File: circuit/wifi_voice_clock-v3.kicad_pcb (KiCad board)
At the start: 2 copper layers, 38.1 x 220.3 mm, 77 parts, among them J1 PinSocket 1x06 5.7mm, J11 PinHeader 1x10 7.7mm, J12 PinHeader 1x10 7.7mm, J13 PinSocket 1x10 3.5mm, J14 PinSocket 1x10 3.5mm, J15 PinSocket 1x10 3.5mm, J16 PinSocket 1x10 3.5mm, J2 PinSocket 1x08 5.7mm, J21 PinSocket 1x10 3.5mm, J22 PinSocket 1x10 3.5mm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

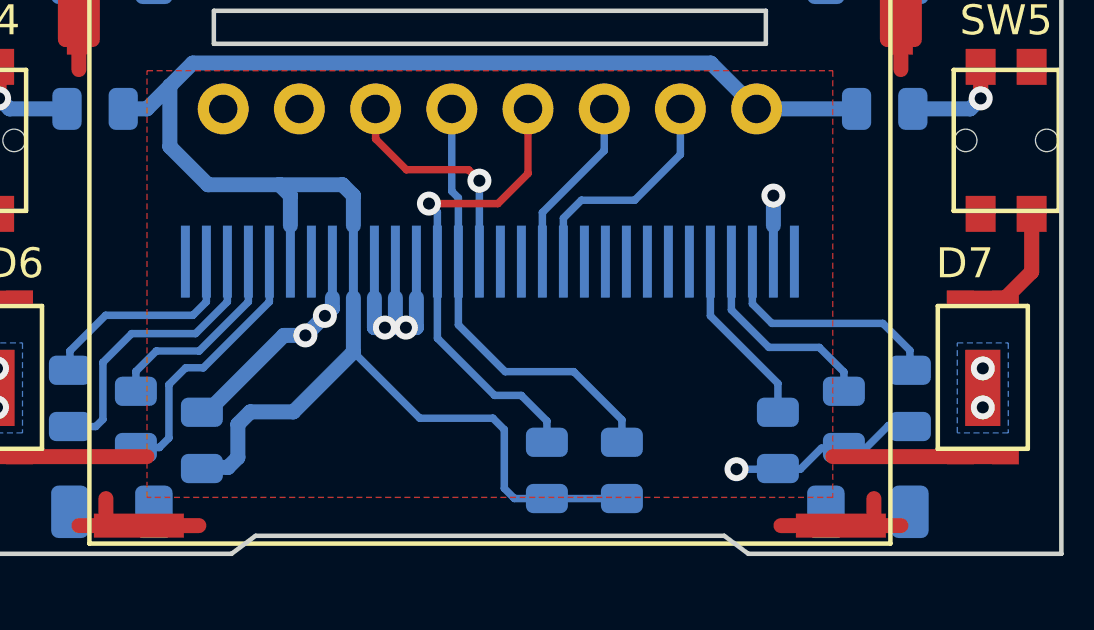
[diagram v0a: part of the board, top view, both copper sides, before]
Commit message: Adjust OLED footprint
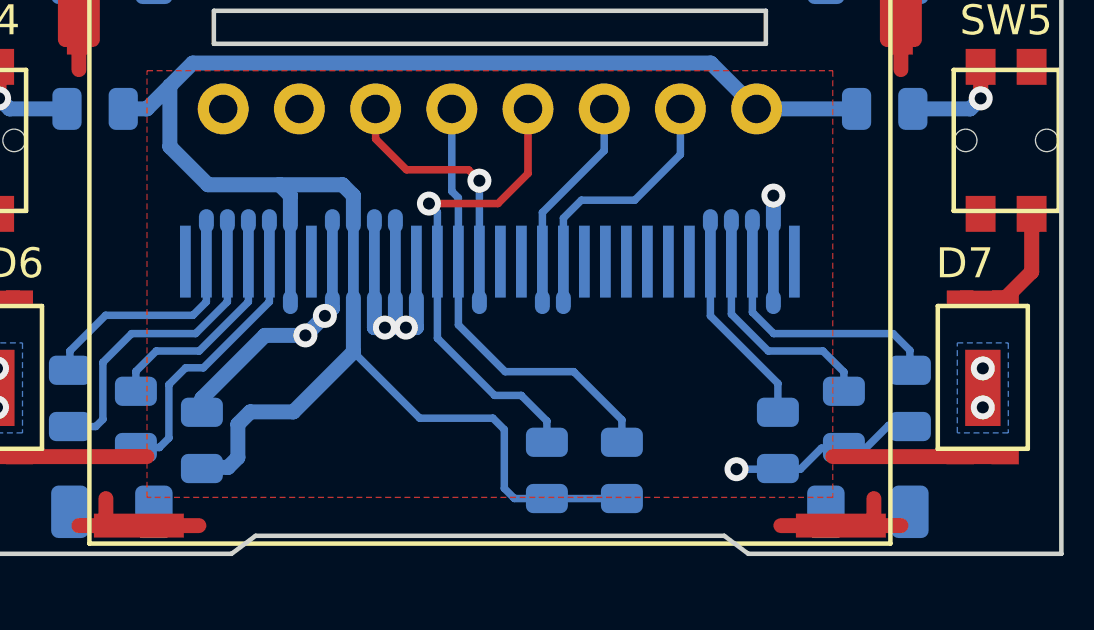
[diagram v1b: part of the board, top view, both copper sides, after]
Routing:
- net /LCD_GND: track 29.5 -> 31.0 mm

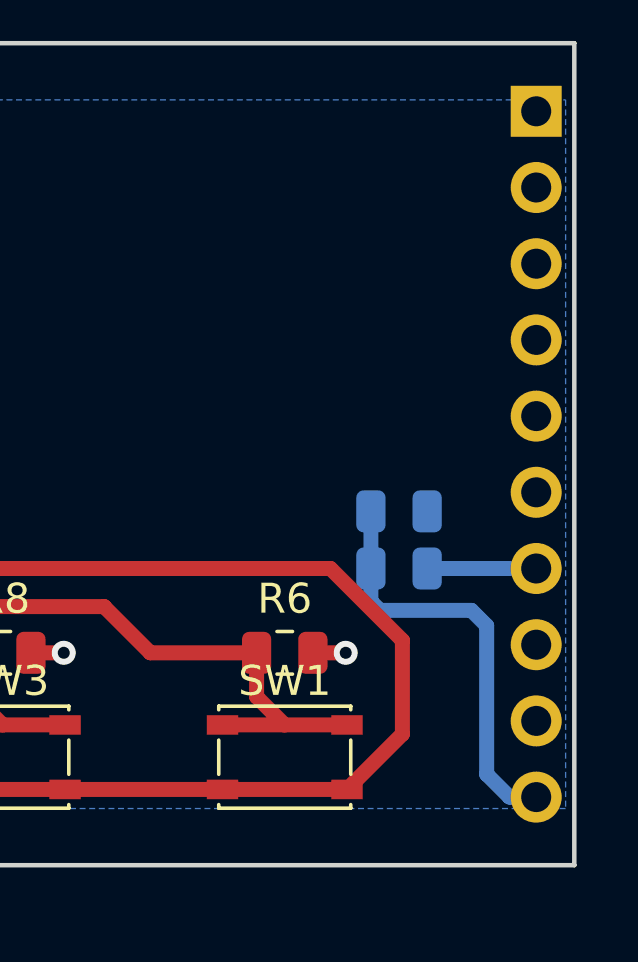
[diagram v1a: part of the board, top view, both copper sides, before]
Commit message: Measure real input voltage
Circuit is from https://jeelabs.org/2013/05/17/zero-powe-battery-measurement/
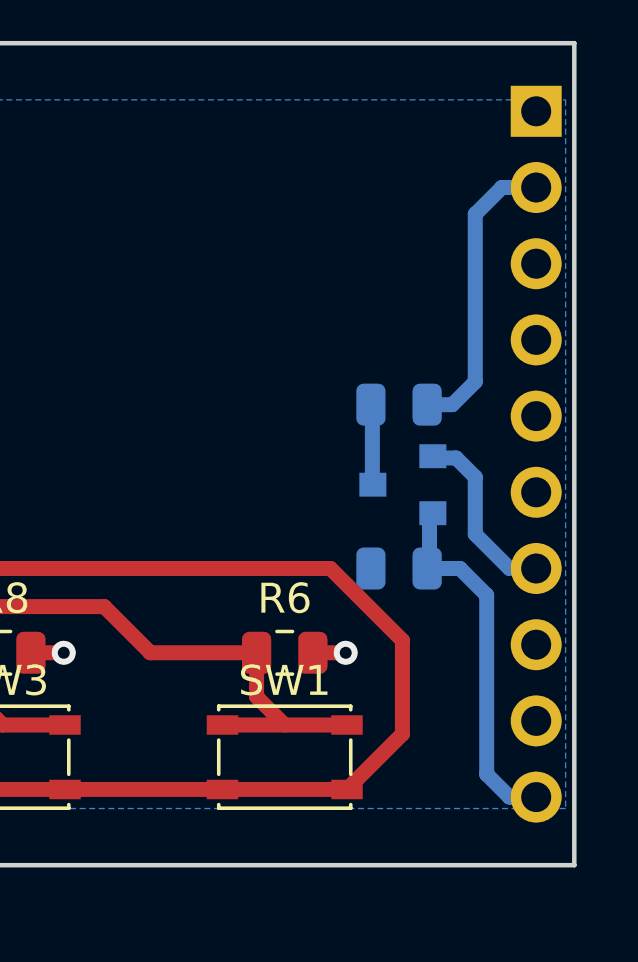
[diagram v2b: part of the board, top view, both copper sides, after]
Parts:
- added Q3: BSS138, Package_TO_SOT_SMD:SOT-23, B.Cu at (13.3, 79.8)
- R9: value 10K -> 40K
- moved R9 5.46 mm to (13.2, 77.1)
- moved R10 1.91 mm to (13.2, 82.5), turned to 0 degrees
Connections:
- R9 pad 1: /CTRL_VMES -> Net-(Q3-Pad3)
- R9 pad 2: /CTRL_VOUT -> /CTRL_VCC
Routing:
- net /CTRL_VCC: track 0.00 -> 9.91 mm
- net Net-(Q3-Pad3): track 0.00 -> 2.67 mm
- net /CTRL_VOUT: track 3.63 -> 6.20 mm
- net /CTRL_VMES: track 14.3 -> 12.1 mm
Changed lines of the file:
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@@
     (thickness 1)
     (drawings 68)
-    (tracks 503)
+    (tracks 511)
     (zones 0)
-    (modules 77)
-    (nets 139)
+    (modules 78)
+    (nets 140)
   )
   (page A4)
@@
   (net 137 "Net-(J22-Pad9)")
   (net 138 "Net-(J22-Pad10)")
+  (net 139 "Net-(Q3-Pad3)")
   (net_class Default "This is the default net class."
     (clearance 0.2)
@@
     (add_net "Net-(LCD1-Pad7)")
     (add_net "Net-(LS1-Pad2)")
+    (add_net "Net-(Q3-Pad3)")
     (add_net "Net-(R15-Pad1)")
     (add_net "Net-(R16-Pad1)")
@@
     )
   )
+  (module Package_TO_SOT_SMD:SOT-23 (layer B.Cu)
+    (at 13.335 79.756 180)
+    (descr "SOT-23, Standard")
+    (tags SOT-23)
+    (attr smd)
+    (fp_text reference Q3 (at 3.175 0 180) (layer B.SilkS)
+      (effects (font (size 1 1) (thickness 0.15)) (justify mirror))
+    )
+    (fp_text value BSS138 (at 0 -2.5 180) (layer B.Fab)
+      (effects (font (size 1 1) (thickness 0.15)) (justify mirror))
+    )
+    (fp_text user %R (at 0 0 90) (layer B.Fab)
+      (effects (font (size 0.5 0.5) (thickness 0.075)) (justify mirror))
+    )
+    (fp_line (start -0.7 0.95) (end -0.7 -1.5) (layer B.Fab) (width 0.1))
+    (fp_line (start -0.15 1.52) (end 0.7 1.52) (layer B.Fab) (width 0.1))
+    (fp_line (start -0.7 0.95) (end -0.15 1.52) (layer B.Fab) (width 0.1))
+    (fp_line (start 0.7 1.52) (end 0.7 -1.52) (layer B.Fab) (width 0.1))
+    (fp_line (start -0.7 -1.52) (end 0.7 -1.52) (layer B.Fab) (width 0.1))
+    (fp_line (start 0.76 -1.58) (end 0.76 -0.65) (layer B.SilkS) (width 0.12))
+    (fp_line (start 0.76 1.58) (end 0.76 0.65) (layer B.SilkS) (width 0.12))
+    (fp_line (start -1.7 1.75) (end 1.7 1.75) (layer B.CrtYd) (width 0.05))
+    (fp_line (start 1.7 1.75) (end 1.7 -1.75) (layer B.CrtYd) (width 0.05))
+    (fp_line (start 1.7 -1.75) (end -1.7 -1.75) (layer B.CrtYd) (width 0.05))
+    (fp_line (start -1.7 -1.75) (end -1.7 1.75) (layer B.CrtYd) (width 0.05))
+    (fp_line (start 0.76 1.58) (end -1.4 1.58) (layer B.SilkS) (width 0.12))
+    (fp_line (start 0.76 -1.58) (end -0.7 -1.58) (layer B.SilkS) (width 0.12))
+    (pad 1 smd rect (at -1 0.95 180) (size 0.9 0.8) (layers B.Cu B.Paste B.Mask)
+      (net 83 /CTRL_VOUT))
+    (pad 2 smd rect (at -1 -0.95 180) (size 0.9 0.8) (layers B.Cu B.Paste B.Mask)
+      (net 82 /CTRL_VMES))
+    (pad 3 smd rect (at 1 0 180) (size 0.9 0.8) (layers B.Cu B.Paste B.Mask)
+      (net 139 "Net-(Q3-Pad3)"))
+    (model ${KISYS3DMOD}/Package_TO_SOT_SMD.3dshapes/SOT-23.wrl
+      (at (xyz 0 0 0))
+      (scale (xyz 1 1 1))
+      (rotate (xyz 0 0 0))
+    )
+  )
   (module Resistor_SMD:R_0805_2012Metric (layer B.Cu)
-    (at 13.208 80.645 180)
+    (at 13.208 82.55)
     (descr "Resistor SMD 0805 (2012 Metric), square (rectangular) end terminal, IPC_7351 nominal, (Body size source: https://docs.google.com/spreadsheets/d/1BsfQQcO9C6DZCsRaXUlFlo91Tg2WpOkGARC1WS5S8t0/edit?usp=sharing), generated with kicad-footprint-generator")
     (tags resistor)
     (attr smd)
-    (fp_text reference R10 (at 3.5 0 unlocked) (layer B.SilkS)
+    (fp_text reference R10 (at -3.5 0 unlocked) (layer B.SilkS)
       (effects (font (size 1 1) (thickness 0.15)) (justify mirror))
     )
-    (fp_text value 10K (at 0 -1.65 180) (layer B.Fab)
+    (fp_text value 10K (at 0 -1.65) (layer B.Fab)
       (effects (font (size 1 1) (thickness 0.15)) (justify mirror))
     )
@@
     (fp_line (start -1 0.6) (end 1 0.6) (layer B.Fab) (width 0.1))
     (fp_line (start -1 -0.6) (end -1 0.6) (layer B.Fab) (width 0.1))
-    (fp_text user %R (at 0 0 180) (layer B.Fab)
+    (fp_text user %R (at 0 0) (layer B.Fab)
       (effects (font (size 0.5 0.5) (thickness 0.08)) (justify mirror))
     )
-    (pad 1 smd roundrect (at -0.9375 0 180) (size 0.975 1.4) (layers B.Cu B.Paste B.Mask) (roundrect_rratio 0.25)
+    (pad 1 smd roundrect (at -0.9375 0) (size 0.975 1.4) (layers B.Cu B.Paste B.Mask) (roundrect_rratio 0.25)
       (net 69 /CTRL_GND))
-    (pad 2 smd roundrect (at 0.9375 0 180) (size 0.975 1.4) (layers B.Cu B.Paste B.Mask) (roundrect_rratio 0.25)
+    (pad 2 smd roundrect (at 0.9375 0) (size 0.975 1.4) (layers B.Cu B.Paste B.Mask) (roundrect_rratio 0.25)
       (net 82 /CTRL_VMES))
     (model ${KISYS3DMOD}/Resistor_SMD.3dshapes/R_0805_2012Metric.wrl
@@
   )
   (module Resistor_SMD:R_0805_2012Metric (layer B.Cu)
-    (at 13.208 82.55)
+    (at 13.208 77.089)
     (descr "Resistor SMD 0805 (2012 Metric), square (rectangular) end terminal, IPC_7351 nominal, (Body size source: https://docs.google.com/spreadsheets/d/1BsfQQcO9C6DZCsRaXUlFlo91Tg2WpOkGARC1WS5S8t0/edit?usp=sharing), generated with kicad-footprint-generator")
     (tags resistor)
@@
       (effects (font (size 1 1) (thickness 0.15)) (justify mirror))
     )
-    (fp_text value 10K (at 0 -1.65) (layer B.Fab)
+    (fp_text value 40K (at 0 -1.65) (layer B.Fab)
       (effects (font (size 1 1) (thickness 0.15)) (justify mirror))
     )
@@
     )
     (pad 1 smd roundrect (at -0.9375 0) (size 0.975 1.4) (layers B.Cu B.Paste B.Mask) (roundrect_rratio 0.25)
-      (net 82 /CTRL_VMES))
+      (net 139 "Net-(Q3-Pad3)"))
     (pad 2 smd roundrect (at 0.9375 0) (size 0.975 1.4) (layers B.Cu B.Paste B.Mask) (roundrect_rratio 0.25)
-      (net 83 /CTRL_VOUT))
+      (net 81 /CTRL_VCC))
     (model ${KISYS3DMOD}/Resistor_SMD.3dshapes/R_0805_2012Metric.wrl
       (at (xyz 0 0 0))
@@
   (segment (start -6.08 90.17) (end -4.572 88.662) (width 0.5) (layer B.Cu) (net 80))
   (segment (start -17.78 90.17) (end -6.08 90.17) (width 0.5) (layer B.Cu) (net 80))
-  (segment (start 12.2705 82.7255) (end 12.2705 80.645) (width 0.5) (layer B.Cu) (net 82))
-  (segment (start 12.2705 83.6445) (end 12.2705 82.55) (width 0.5) (layer B.Cu) (net 82))
-  (segment (start 12.573 83.947) (end 12.2705 83.6445) (width 0.5) (layer B.Cu) (net 82))
-  (segment (start 15.621 83.947) (end 12.573 83.947) (width 0.5) (layer B.Cu) (net 82))
-  (segment (start 16.129 84.455) (end 15.621 83.947) (width 0.5) (layer B.Cu) (net 82))
-  (segment (start 16.129 89.408) (end 16.129 84.455) (width 0.5) (layer B.Cu) (net 82))
-  (segment (start 16.891 90.17) (end 16.129 89.408) (width 0.5) (layer B.Cu) (net 82))
+  (segment (start 14.986 77.089) (end 14.1455 77.089) (width 0.5) (layer B.Cu) (net 81))
+  (segment (start 15.748 76.327) (end 14.986 77.089) (width 0.5) (layer B.Cu) (net 81))
+  (segment (start 15.748 70.739) (end 15.748 76.327) (width 0.5) (layer B.Cu) (net 81))
+  (segment (start 17.78 69.85) (end 16.637 69.85) (width 0.5) (layer B.Cu) (net 81))
+  (segment (start 16.637 69.85) (end 15.748 70.739) (width 0.5) (layer B.Cu) (net 81))
+  (segment (start 16.129 83.439) (end 15.24 82.55) (width 0.5) (layer B.Cu) (net 82))
+  (segment (start 15.24 82.55) (end 14.097 82.55) (width 0.5) (layer B.Cu) (net 82))
+  (segment (start 16.129 89.408) (end 16.129 83.439) (width 0.5) (layer B.Cu) (net 82))
   (segment (start 17.78 90.17) (end 16.891 90.17) (width 0.5) (layer B.Cu) (net 82))
-  (segment (start 17.78 82.55) (end 14.1455 82.55) (width 0.5) (layer B.Cu) (net 83))
+  (segment (start 16.891 90.17) (end 16.129 89.408) (width 0.5) (layer B.Cu) (net 82))
+  (segment (start 14.224 80.772) (end 14.224 82.55) (width 0.5) (layer B.Cu) (net 82))
+  (segment (start 16.891 82.55) (end 17.78 82.55) (width 0.5) (layer B.Cu) (net 83))
+  (segment (start 15.748 79.502) (end 15.748 81.407) (width 0.5) (layer B.Cu) (net 83))
+  (segment (start 15.748 81.407) (end 16.891 82.55) (width 0.5) (layer B.Cu) (net 83))
+  (segment (start 14.224 78.867) (end 15.113 78.867) (width 0.5) (layer B.Cu) (net 83))
+  (segment (start 15.113 78.867) (end 15.748 79.502) (width 0.5) (layer B.Cu) (net 83))
   (segment (start -12.2705 82.55) (end -12.2705 79.05) (width 0.5) (layer B.Cu) (net 87))
   (via (at -14.72 74.549) (size 0.8) (drill 0.4) (layers F.Cu B.Cu) (net 88))
@@
   (segment (start 8.89 209.45) (end 8.89 212.58) (width 0.75) (layer B.Cu) (net 137))
   (segment (start 11.43 209.45) (end 11.43 212.58) (width 0.75) (layer B.Cu) (net 138))
+  (segment (start 12.319 77.089) (end 12.319 79.756) (width 0.5) (layer B.Cu) (net 139))
   (zone (net 69) (net_name /CTRL_GND) (layer B.Cu) (hatch edge 0.508)
     (connect_pads (clearance 0.508))

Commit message: Update pcb version and gerber to 3.3
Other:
- board text added: "V3.3"
- board text removed: "V3.2"
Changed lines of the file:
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@@
   (gr_line (start -8.612 154.28) (end -19.05 154.28) (layer Edge.Cuts) (width 0.15))
   (gr_line (start -19.05 154.28) (end -19.05 133.68) (layer Edge.Cuts) (width 0.15))
-  (gr_text V3.2 (at 0 1.4) (layer F.SilkS)
+  (gr_text V3.3 (at 0 1.4) (layer F.SilkS)
     (effects (font (size 1.5 1.5) (thickness 0.3)))
   )
